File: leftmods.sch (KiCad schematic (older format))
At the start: 16 parts

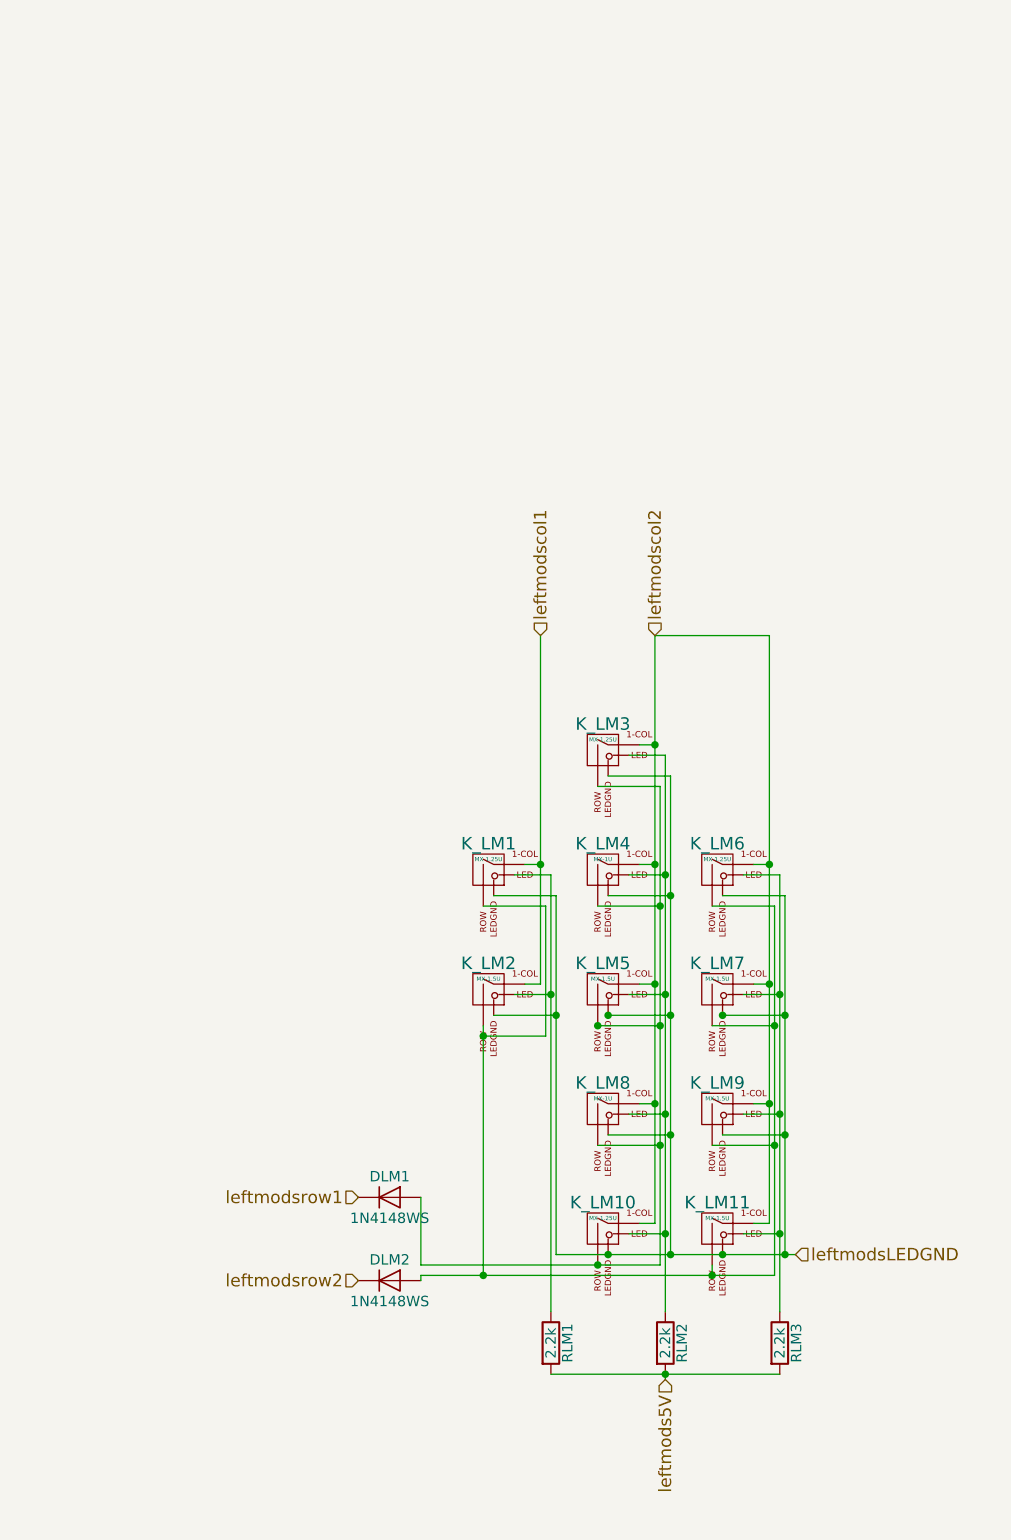
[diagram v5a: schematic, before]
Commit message: Revert "Fix left mods diode location"
This reverts commit 3448258528d86bfc7727b0cdfdec81eb2e658ed9.
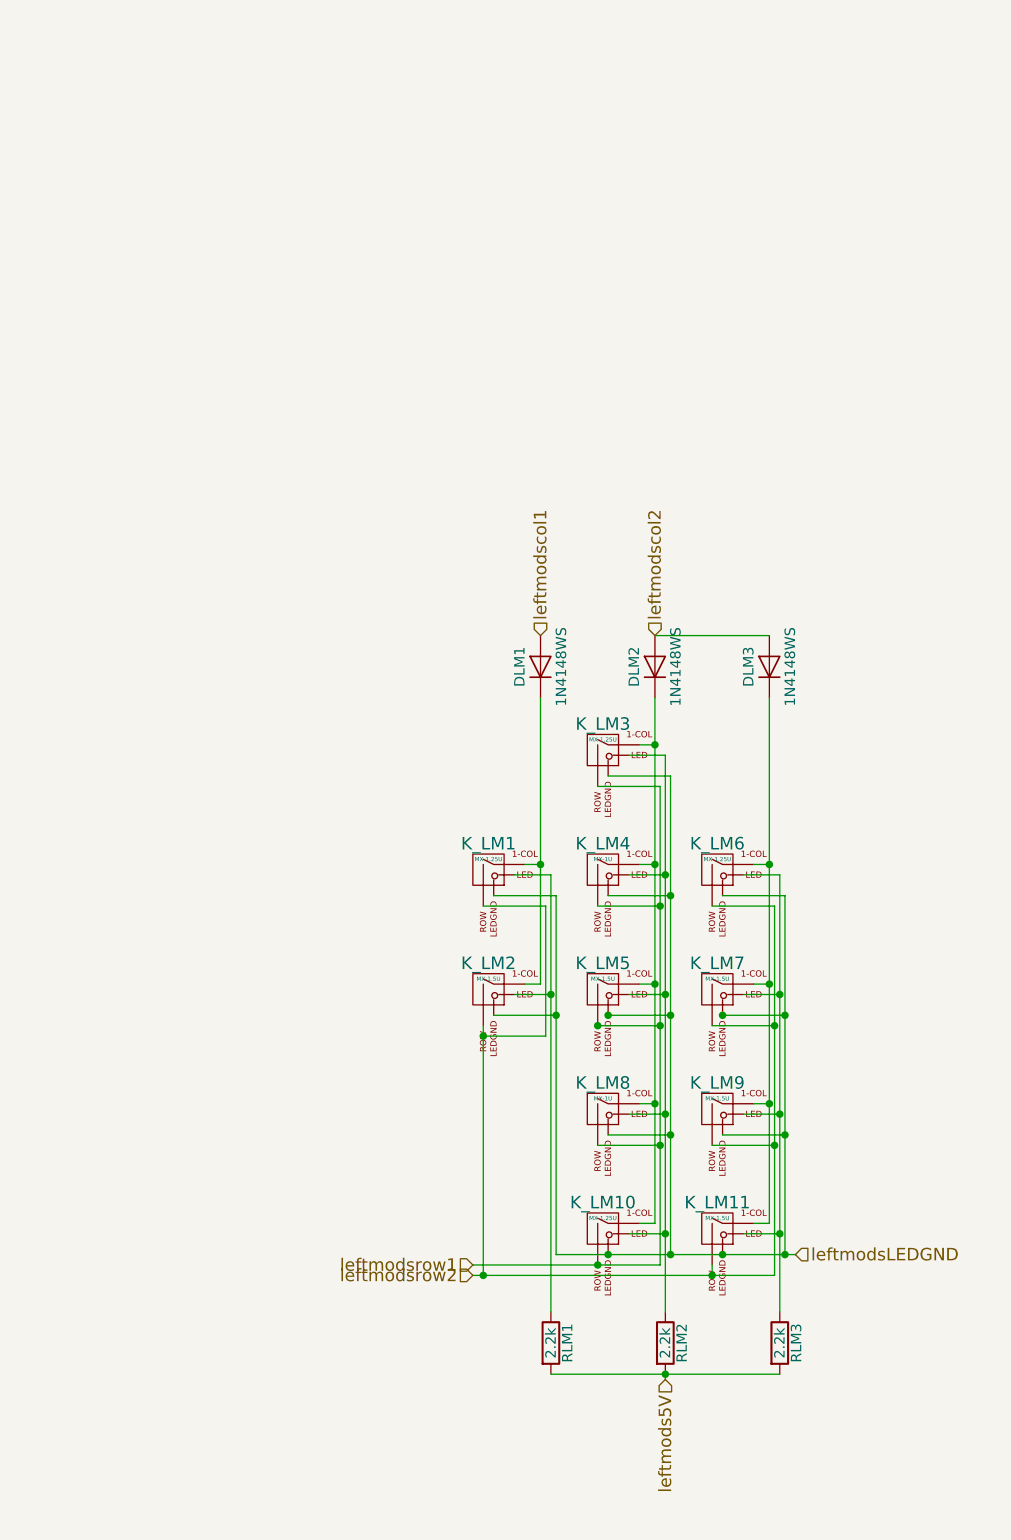
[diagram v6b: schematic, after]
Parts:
- added DLM3: 1N4148WS, symbol D
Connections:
- net leftmodscol1: now also DLM1.2 (A); no longer K_LM1.1 (COL), K_LM2.1 (COL)
- net leftmodscol2: now also DLM2.2 (A), DLM3.2 (A); no longer K_LM10.1 (COL), K_LM11.1 (COL), K_LM3.1 (COL), K_LM4.1 (COL), K_LM5.1 (COL), K_LM6.1 (COL), K_LM7.1 (COL), K_LM8.1 (COL), K_LM9.1 (COL)
- net leftmodsrow1: now also K_LM10.2 (ROW), K_LM3.2 (ROW), K_LM4.2 (ROW), K_LM5.2 (ROW), K_LM8.2 (ROW); no longer DLM1.1 (K)
- net leftmodsrow2: now also K_LM1.2 (ROW), K_LM11.2 (ROW), K_LM2.2 (ROW), K_LM6.2 (ROW), K_LM7.2 (ROW), K_LM9.2 (ROW); no longer DLM2.1 (K)
- new net: DLM1.1 (K), K_LM1.1 (COL), K_LM2.1 (COL)
- new net: DLM2.1 (K), K_LM10.1 (COL), K_LM3.1 (COL), K_LM4.1 (COL), K_LM5.1 (COL), K_LM8.1 (COL)
- new net: DLM3.1 (K), K_LM11.1 (COL), K_LM6.1 (COL), K_LM7.1 (COL), K_LM9.1 (COL)
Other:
- moved on the sheet: DLM1, DLM2
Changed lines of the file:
@@
 	1    0    0    -1
 $EndComp
-Text HLabel 3625 6275 0    60   Input ~ 0
+Text HLabel 4175 6600 0    60   Input ~ 0
 leftmodsrow1
 $Comp
 L D DLM1
 U 1 1 591D216C
-P 3775 6275
-F 0 "DLM1" H 3775 6375 50  0000 C CNN
-F 1 "1N4148WS" H 3775 6175 50  0000 C CNN
-F 2 "" H 3775 6275 50  0001 C CNN
-F 3 "" H 3775 6275 50  0000 C CNN
-	1    3775 6275
-	1    0    0    -1
+P 4500 3725
+F 0 "DLM1" H 4500 3825 50  0000 C CNN
+F 1 "1N4148WS" H 4500 3625 50  0000 C CNN
+F 2 "" H 4500 3725 50  0001 C CNN
+F 3 "" H 4500 3725 50  0000 C CNN
+	1    4500 3725
+	0    -1   -1   0
 $EndComp
 $Comp
 L D DLM2
 U 1 1 591D28A1
-P 3775 6675
-F 0 "DLM2" H 3775 6775 50  0000 C CNN
-F 1 "1N4148WS" H 3775 6575 50  0000 C CNN
-F 2 "" H 3775 6675 50  0001 C CNN
-F 3 "" H 3775 6675 50  0000 C CNN
-	1    3775 6675
-	1    0    0    -1
+P 5050 3725
+F 0 "DLM2" H 5050 3825 50  0000 C CNN
+F 1 "1N4148WS" H 5050 3625 50  0000 C CNN
+F 2 "" H 5050 3725 50  0001 C CNN
+F 3 "" H 5050 3725 50  0000 C CNN
+	1    5050 3725
+	0    -1   -1   0
+$EndComp
+$Comp
+L D DLM3
+U 1 1 591D2AA8
+P 5600 3725
+F 0 "DLM3" H 5600 3825 50  0000 C CNN
+F 1 "1N4148WS" H 5600 3625 50  0000 C CNN
+F 2 "" H 5600 3725 50  0001 C CNN
+F 3 "" H 5600 3725 50  0000 C CNN
+	1    5600 3725
+	0    -1   -1   0
 $EndComp
 Text HLabel 4500 3575 1    60   Input ~ 0
@@
 Text HLabel 5100 7150 3    60   Input ~ 0
 leftmods5V
-Text HLabel 3625 6675 0    60   Input ~ 0
+Text HLabel 4175 6650 0    60   Input ~ 0
 leftmodsrow2
 $Comp
@@
 	4500 5250 4425 5250
 Wire Wire Line
-	4500 3575 4500 5250
+	4500 3875 4500 5250
 Wire Wire Line
 	4425 4675 4500 4675
@@
 	5600 5250 5525 5250
 Wire Wire Line
-	5600 3575 5600 6400
+	5600 3875 5600 6400
 Wire Wire Line
 	5525 4675 5600 4675
@@
 	5050 4675 4975 4675
 Wire Wire Line
-	5050 3575 5050 6400
+	5050 3875 5050 6400
 Wire Wire Line
 	4975 4100 5050 4100
@@
 	5325 6650 5325 6600
 Wire Wire Line
-	3925 6650 5625 6650
+	4175 6650 5625 6650
 Connection ~ 4225 6650
 Wire Wire Line
-	3925 6600 5075 6600
+	4175 6600 5075 6600
 Connection ~ 5075 6025
 Connection ~ 4775 6600
@@
 	5375 5975 5675 5975
 Connection ~ 5675 5975
-Wire Wire Line
-	3925 6275 3925 6600
-Wire Wire Line
-	3925 6675 3925 6650
 $EndSCHEMATC

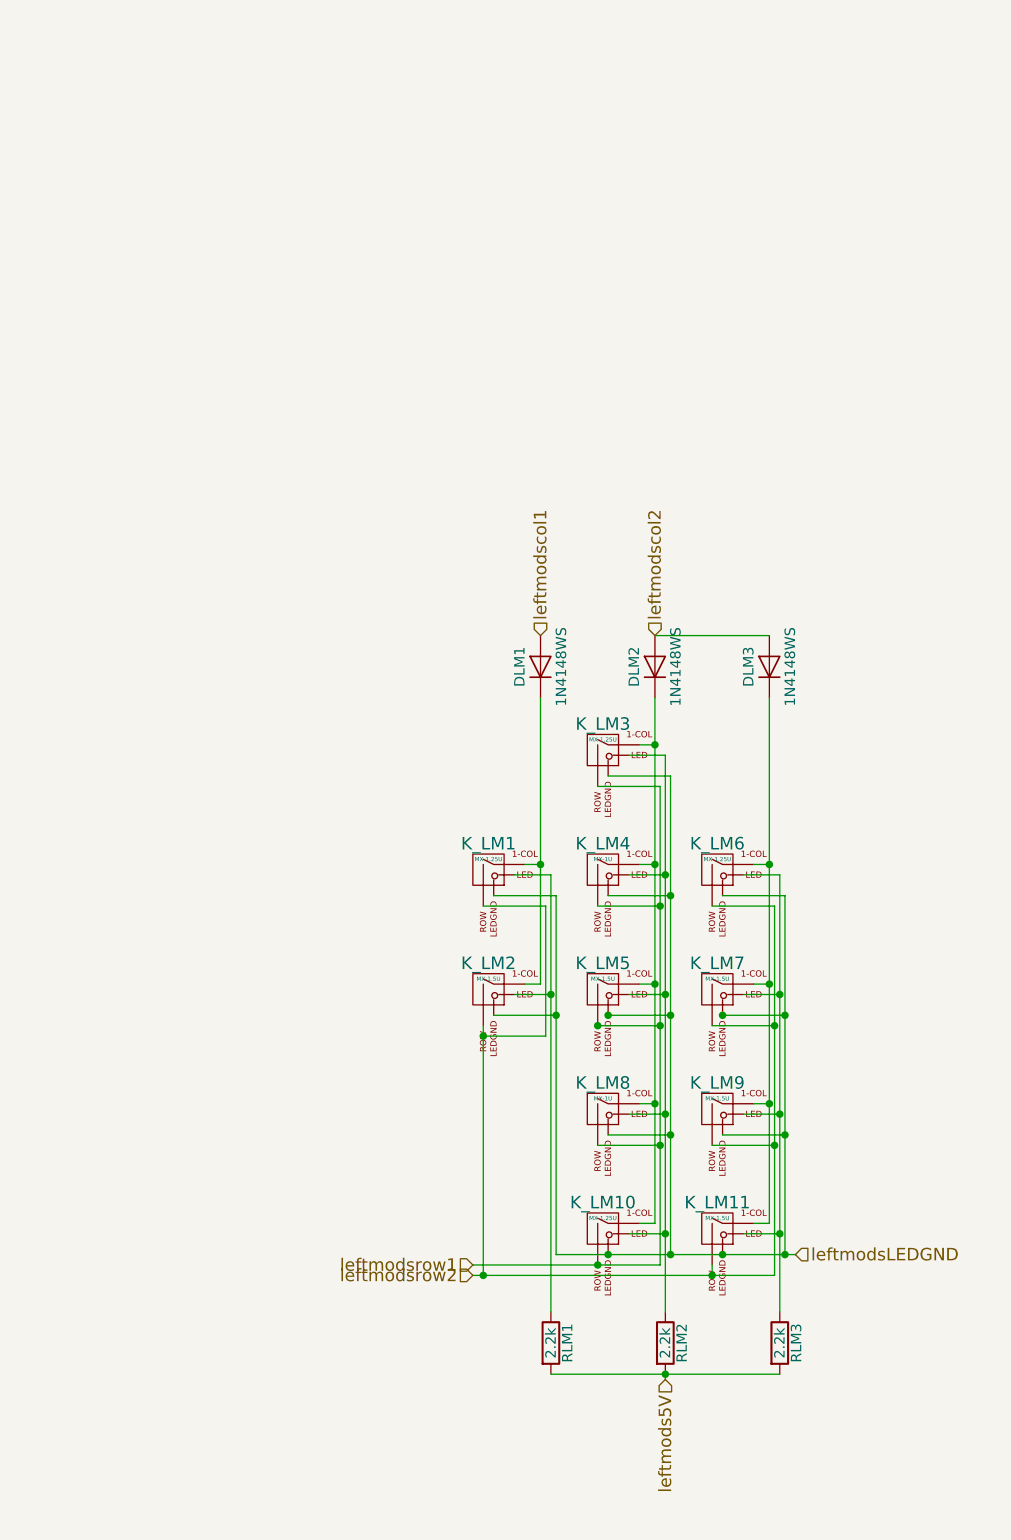
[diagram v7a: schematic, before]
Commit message: Fix LMods Diode Location
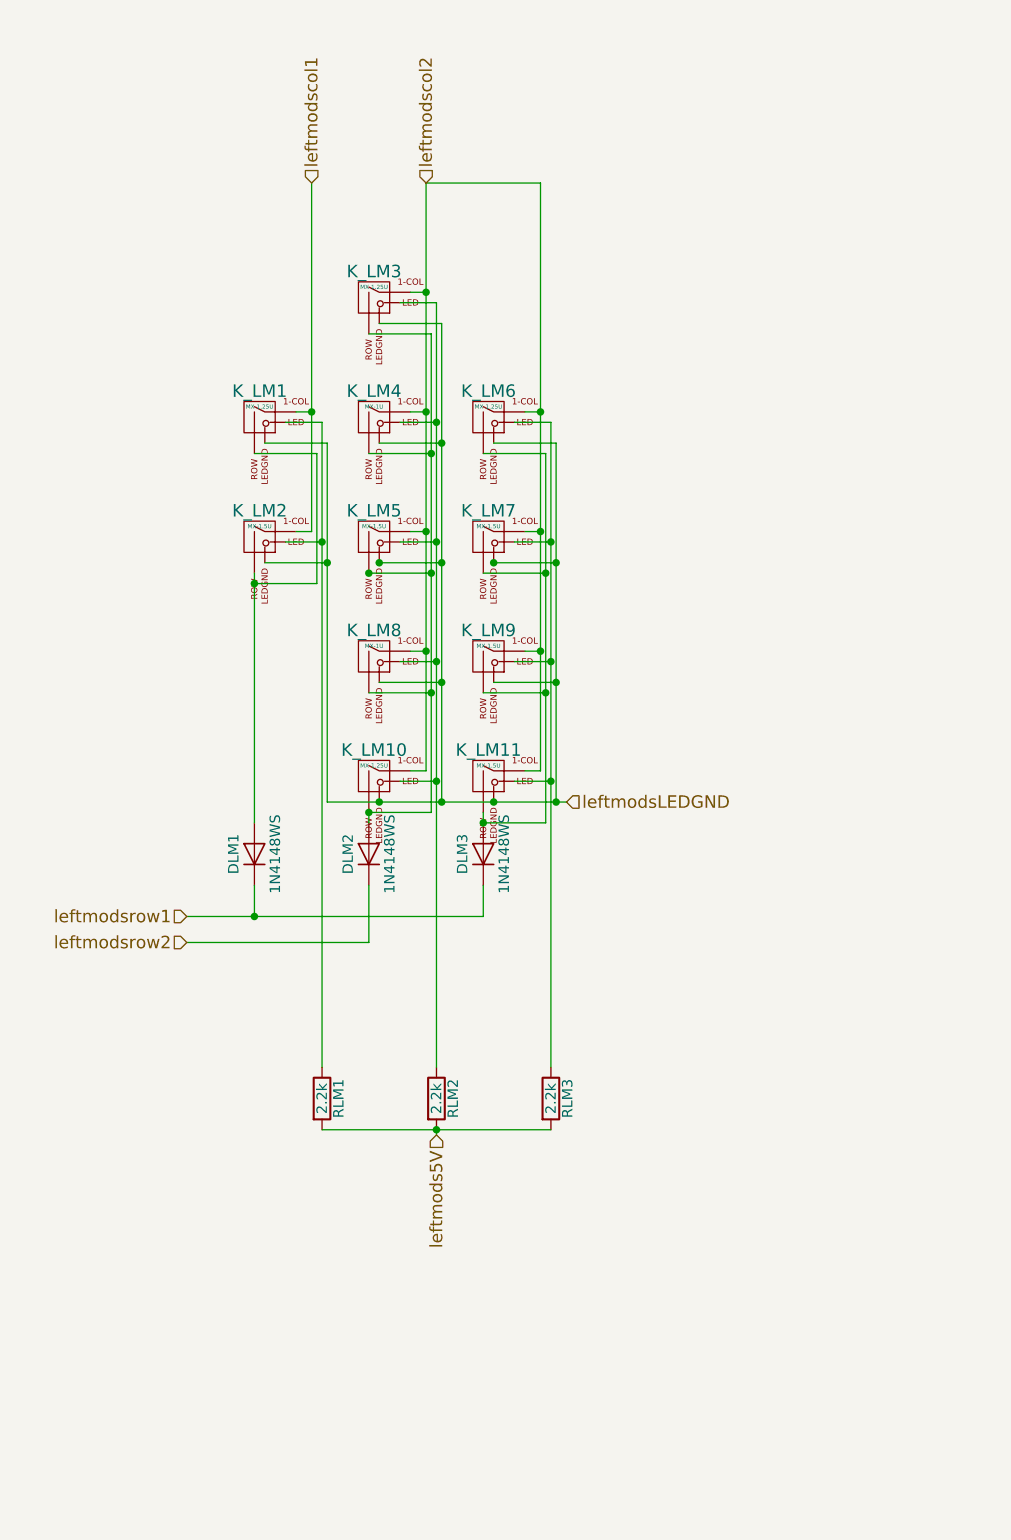
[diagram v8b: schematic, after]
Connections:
- net leftmodscol1: now also K_LM1.1 (COL), K_LM2.1 (COL); no longer DLM1.2 (A)
- net leftmodscol2: now also K_LM10.1 (COL), K_LM11.1 (COL), K_LM3.1 (COL), K_LM4.1 (COL), K_LM5.1 (COL), K_LM6.1 (COL), K_LM7.1 (COL), K_LM8.1 (COL), K_LM9.1 (COL); no longer DLM2.2 (A), DLM3.2 (A)
- net leftmodsrow1: now also DLM1.1 (K), DLM3.1 (K); no longer K_LM10.2 (ROW), K_LM3.2 (ROW), K_LM4.2 (ROW), K_LM5.2 (ROW), K_LM8.2 (ROW)
- net leftmodsrow2: now also DLM2.1 (K); no longer K_LM1.2 (ROW), K_LM11.2 (ROW), K_LM2.2 (ROW), K_LM6.2 (ROW), K_LM7.2 (ROW), K_LM9.2 (ROW)
- new net: DLM1.2 (A), K_LM1.2 (ROW), K_LM2.2 (ROW)
- new net: DLM2.2 (A), K_LM10.2 (ROW), K_LM3.2 (ROW), K_LM4.2 (ROW), K_LM5.2 (ROW), K_LM8.2 (ROW)
- new net: DLM3.2 (A), K_LM11.2 (ROW), K_LM6.2 (ROW), K_LM7.2 (ROW), K_LM9.2 (ROW)
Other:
- moved on the sheet: DLM1, DLM2, DLM3, K_LM1, K_LM10, K_LM11, K_LM2, K_LM3, K_LM4, K_LM5, K_LM6, K_LM7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
